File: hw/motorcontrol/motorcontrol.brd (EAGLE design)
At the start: 65 x 58 mm, 105 parts, among them J2 USB-MICROB, U1 BTN8982TA, U10 BSS138BKS, U11 DMG2305UX, U12 BSS138BKS, U2 BTN8982TA, U3 BTN8982TA, U4 CAT24C32WI-GT3, U5 ADG3304, U6 MMDT5401, U7 PTR08060W, U8 IPD90P03P4L-04, U9 ATMEGA32U4

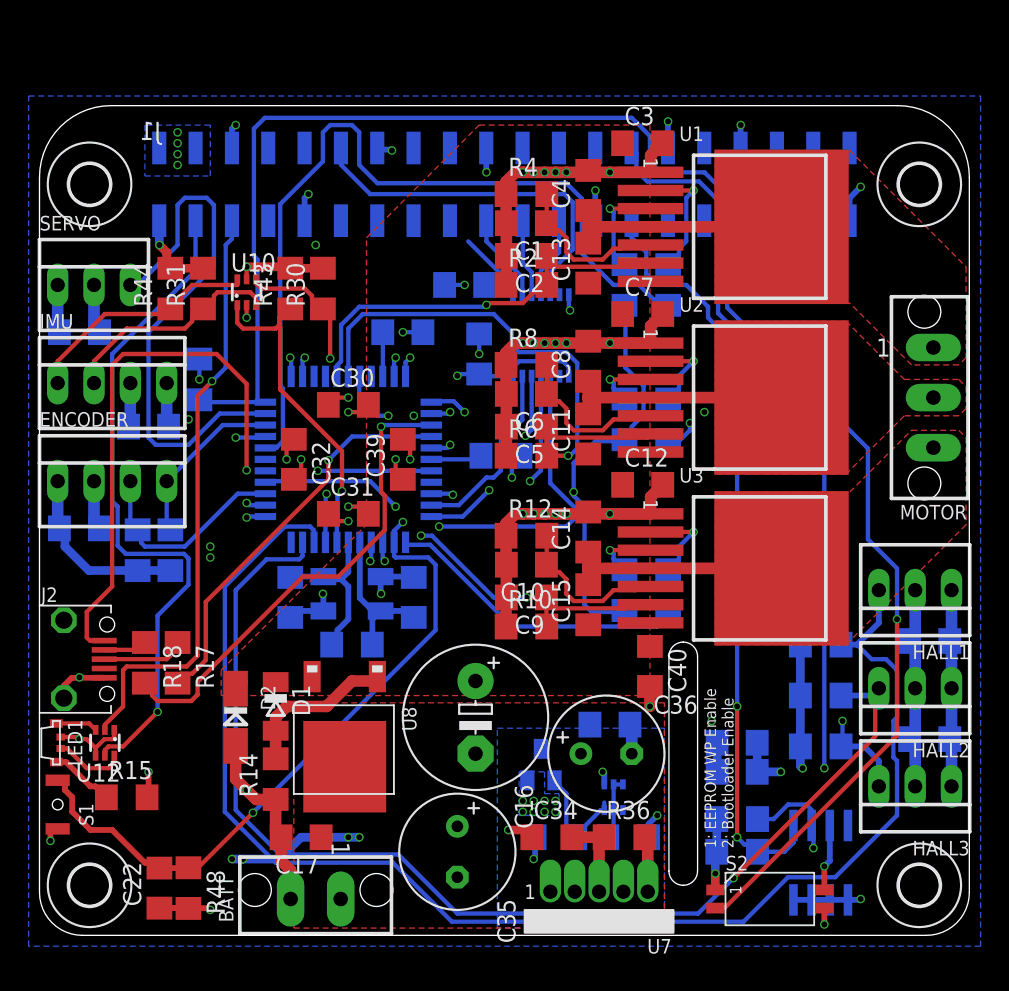
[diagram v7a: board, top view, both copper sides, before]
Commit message: board is completely routed and checked
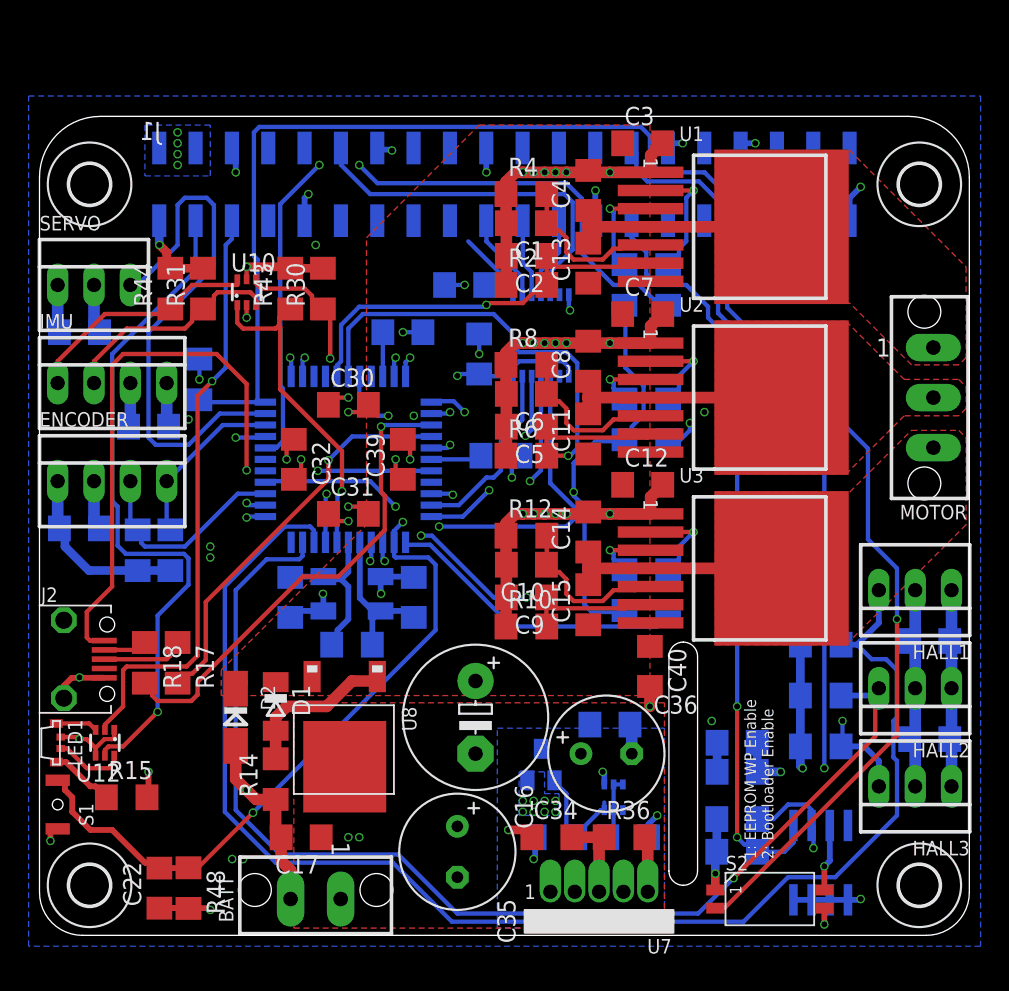
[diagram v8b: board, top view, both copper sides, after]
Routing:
- net D9: track 57.5 -> 52.6 mm, vias 0 -> 2
- net GND: track 173.8 -> 172.8 mm
- net N$8: track 121.0 -> 120.3 mm
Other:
- board size 65 x 58 mm -> 65 x 57.2 mm
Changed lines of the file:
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@@
 <setting verticaltext="up"/>
 </settings>
-<grid distance="10" unitdist="mil" unit="mil" style="dots" multiple="1" display="yes" altdistance="2.5" altunitdist="mil" altunit="mil"/>
+<grid distance="10" unitdist="mil" unit="mm" style="dots" multiple="1" display="yes" altdistance="2.5" altunitdist="mil" altunit="mil"/>
 <layers>
-<layer number="1" name="Top" color="4" fill="1" visible="no" active="yes"/>
+<layer number="1" name="Top" color="4" fill="1" visible="yes" active="yes"/>
 <layer number="2" name="Route2" color="6" fill="1" visible="no" active="yes"/>
 <layer number="3" name="Route3" color="4" fill="3" visible="no" active="no"/>
 <layer number="14" name="Route14" color="1" fill="6" visible="no" active="no"/>
 <layer number="15" name="Route15" color="3" fill="1" visible="no" active="yes"/>
-<layer number="16" name="Bottom" color="1" fill="1" visible="no" active="yes"/>
+<layer number="16" name="Bottom" color="1" fill="1" visible="yes" active="yes"/>
 <layer number="17" name="Pads" color="2" fill="1" visible="yes" active="yes"/>
 <layer number="18" name="Vias" color="2" fill="1" visible="yes" active="yes"/>
@@
 <plain>
 <wire x1="65" y1="3" x2="65" y2="53" width="0" layer="20"/>
-<wire x1="65" y1="53" x2="60" y2="58" width="0" layer="20" curve="90"/>
-<wire x1="60" y1="58" x2="5" y2="58" width="0" layer="20"/>
-<wire x1="5" y1="58" x2="0" y2="53" width="0" layer="20" curve="90"/>
+<wire x1="65" y1="53" x2="60.75" y2="57.25" width="0" layer="20" curve="90"/>
+<wire x1="60.75" y1="57.25" x2="4.25" y2="57.25" width="0" layer="20"/>
+<wire x1="4.25" y1="57.25" x2="0" y2="53" width="0" layer="20" curve="90"/>
 <wire x1="0" y1="53" x2="0" y2="3" width="0" layer="20"/>
 <wire x1="0" y1="3" x2="3" y2="0" width="0" layer="20" curve="90"/>
@@
 <wire x1="44" y1="19.5" x2="45" y2="20.5" width="0" layer="20" curve="-90"/>
 <wire x1="45" y1="20.5" x2="46" y2="19.5" width="0" layer="20" curve="-90"/>
-<text x="48.514" y="6.096" size="0.8128" layer="21" rot="R90">1: EEPROM WP Enable
+<text x="51.308" y="5.334" size="0.8128" layer="21" rot="R90">1: EEPROM WP Enable
 2: Bootloader Enable</text>
 </plain>
@@
 <wire x1="56.63" y1="51.55" x2="57.404" y2="52.324" width="0.4064" layer="16"/>
 <via x="57.404" y="52.324" extent="1-16" drill="0.4064"/>
-<wire x1="49.01" y1="55.04" x2="49.01" y2="56.63" width="0.4064" layer="16"/>
-<wire x1="49.01" y1="56.63" x2="49.022" y2="56.642" width="0.4064" layer="16"/>
-<via x="49.022" y="56.642" extent="1-16" drill="0.4064"/>
-<wire x1="43.93" y1="55.04" x2="43.93" y2="56.884" width="0.4064" layer="16"/>
-<wire x1="43.93" y1="56.884" x2="43.942" y2="56.896" width="0.4064" layer="16"/>
-<via x="43.942" y="56.896" extent="1-16" drill="0.4064"/>
+<via x="50.038" y="55.372" extent="1-16" drill="0.4064"/>
+<via x="44.958" y="55.372" extent="1-16" drill="0.4064"/>
 <wire x1="24.5745" y1="54.9275" x2="24.638" y2="54.864" width="0.4064" layer="16"/>
 <wire x1="31.23" y1="55.04" x2="31.23" y2="53.352" width="0.4064" layer="16"/>
@@
 <wire x1="18.53" y1="51.55" x2="18.796" y2="51.816" width="0.4064" layer="16"/>
 <via x="18.796" y="51.816" extent="1-16" drill="0.4064"/>
-<wire x1="13.45" y1="55.04" x2="13.45" y2="56.376" width="0.4064" layer="16"/>
-<wire x1="13.45" y1="56.376" x2="13.716" y2="56.642" width="0.4064" layer="16"/>
-<via x="13.716" y="56.642" extent="1-16" drill="0.4064"/>
+<via x="13.716" y="53.34" extent="1-16" drill="0.4064"/>
 <wire x1="38.85" y1="49.96" x2="38.85" y2="52.058" width="0.4064" layer="16"/>
 <wire x1="38.85" y1="52.058" x2="38.862" y2="52.07" width="0.4064" layer="16"/>
@@
 <via x="29.718" y="45.466" extent="1-16" drill="0.4064"/>
 <via x="14.478" y="10.16" extent="1-16" drill="0.4064"/>
+<wire x1="44.958" y1="55.372" x2="44.262" y2="55.372" width="0.4064" layer="16"/>
+<wire x1="44.262" y1="55.372" x2="43.93" y2="55.04" width="0.4064" layer="16"/>
+<wire x1="13.716" y1="53.34" x2="13.716" y2="54.774" width="0.4064" layer="16"/>
+<wire x1="13.716" y1="54.774" x2="13.45" y2="55.04" width="0.4064" layer="16"/>
+<wire x1="50.038" y1="55.372" x2="49.342" y2="55.372" width="0.4064" layer="16"/>
+<wire x1="49.342" y1="55.372" x2="49.01" y2="55.04" width="0.4064" layer="16"/>
 </signal>
 <signal name="N$6">
@@
 <wire x1="7.112" y1="36.068" x2="7.112" y2="37.846" width="0.6096" layer="15"/>
 <via x="11.938" y="27.178" extent="1-16" drill="0.4064"/>
-<wire x1="13.462" y1="5.334" x2="14.224" y2="5.334" width="0.6096" layer="16"/>
-<wire x1="14.224" y1="5.334" x2="16.764" y2="5.334" width="0.6096" layer="16"/>
-<wire x1="16.764" y1="5.334" x2="18.288" y2="6.858" width="0.6096" layer="16"/>
-<wire x1="18.288" y1="6.858" x2="21.59" y2="6.858" width="0.6096" layer="16"/>
+<wire x1="13.462" y1="5.334" x2="14.224" y2="5.334" width="0.6096" layer="15"/>
+<wire x1="14.224" y1="5.334" x2="16.764" y2="5.334" width="0.6096" layer="15"/>
+<wire x1="16.764" y1="5.334" x2="18.288" y2="6.858" width="0.6096" layer="15"/>
+<wire x1="18.288" y1="6.858" x2="21.59" y2="6.858" width="0.6096" layer="15"/>
+<wire x1="21.59" y1="6.858" x2="22.352" y2="6.858" width="0.6096" layer="15"/>
 <via x="13.462" y="5.334" extent="1-16" drill="0.4064"/>
 <via x="14.224" y="5.334" extent="1-16" drill="0.4064"/>
 <via x="22.352" y="6.858" extent="1-16" drill="0.4064"/>
-<wire x1="21.59" y1="6.858" x2="22.352" y2="6.858" width="0.6096" layer="16"/>
 <via x="21.59" y="6.858" extent="1-16" drill="0.4064"/>
 </signal>
@@
 <contactref element="R3" pad="1"/>
 <wire x1="16.8275" y1="51.1175" x2="16.8275" y2="38.4175" width="0.3048" layer="16"/>
-<wire x1="19.812" y1="54.102" x2="16.8275" y2="51.1175" width="0.3048" layer="16"/>
+<wire x1="19.558" y1="53.848" x2="16.8275" y2="51.1175" width="0.3048" layer="16"/>
 <wire x1="23.622" y1="52.578" x2="22.352" y2="53.848" width="0.3048" layer="16"/>
 <wire x1="36.83" y1="52.578" x2="23.622" y2="52.578" width="0.3048" layer="16"/>
@@
 <wire x1="42.926" y1="44.45" x2="41.91" y2="45.466" width="0.3048" layer="16"/>
 <wire x1="40.132" y1="45.466" x2="41.91" y2="45.466" width="0.3048" layer="16"/>
-<wire x1="19.812" y1="54.102" x2="19.812" y2="56.134" width="0.3048" layer="16"/>
-<wire x1="19.812" y1="56.134" x2="20.32" y2="56.642" width="0.3048" layer="16"/>
-<wire x1="20.32" y1="56.642" x2="21.844" y2="56.642" width="0.3048" layer="16"/>
-<wire x1="21.844" y1="56.642" x2="22.352" y2="56.134" width="0.3048" layer="16"/>
-<wire x1="22.352" y1="56.134" x2="22.352" y2="53.848" width="0.3048" layer="16"/>
+<via x="19.558" y="53.848" extent="1-16" drill="0.4064"/>
+<wire x1="19.558" y1="53.848" x2="22.352" y2="53.848" width="0.3048" layer="15"/>
+<via x="22.352" y="53.848" extent="1-16" drill="0.4064"/>
 </signal>
 <signal name="D8">
@@
 <wire x1="42.672" y1="54.102" x2="43.434" y2="53.34" width="0.3048" layer="16"/>
 <wire x1="42.672" y1="55.88" x2="42.672" y2="54.102" width="0.3048" layer="16"/>
-<wire x1="41.402" y1="57.15" x2="42.672" y2="55.88" width="0.3048" layer="16"/>
+<wire x1="42.037" y1="56.515" x2="42.672" y2="55.88" width="0.3048" layer="16"/>
 <wire x1="15.24" y1="37.274" x2="15.24" y2="47.244" width="0.3048" layer="16"/>
 <wire x1="15.24" y1="47.244" x2="14.986" y2="47.498" width="0.3048" layer="16"/>
-<wire x1="14.986" y1="47.498" x2="14.986" y2="56.388" width="0.3048" layer="16"/>
+<wire x1="14.986" y1="47.498" x2="14.986" y2="56.134" width="0.3048" layer="16"/>
 <via x="59.944" y="22.098" extent="1-16" drill="0.4064"/>
 <wire x1="47.244" y1="1.905" x2="47.879" y2="1.905" width="0.3048" layer="1"/>
 <wire x1="47.879" y1="1.905" x2="59.944" y2="13.97" width="0.3048" layer="1"/>
-<wire x1="14.986" y1="56.388" x2="15.748" y2="57.15" width="0.3048" layer="16"/>
-<wire x1="15.748" y1="57.15" x2="41.402" y2="57.15" width="0.3048" layer="16"/>
+<wire x1="14.986" y1="56.134" x2="15.367" y2="56.515" width="0.3048" layer="16"/>
+<wire x1="15.367" y1="56.515" x2="42.037" y2="56.515" width="0.3048" layer="16"/>
 </signal>
 <signal name="N$10">
